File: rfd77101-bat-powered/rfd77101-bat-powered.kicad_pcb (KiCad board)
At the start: 2 copper layers, 23 parts, among them J1 USB_OTG, J2 BATT_CONN, J3 Conn_01x07, Q1 Q_NMOS_GSD, Q2 Q_PMOS_GSD, U1 RFD77101, U2 MCP73811T-420I-OT, U3 TLV74130

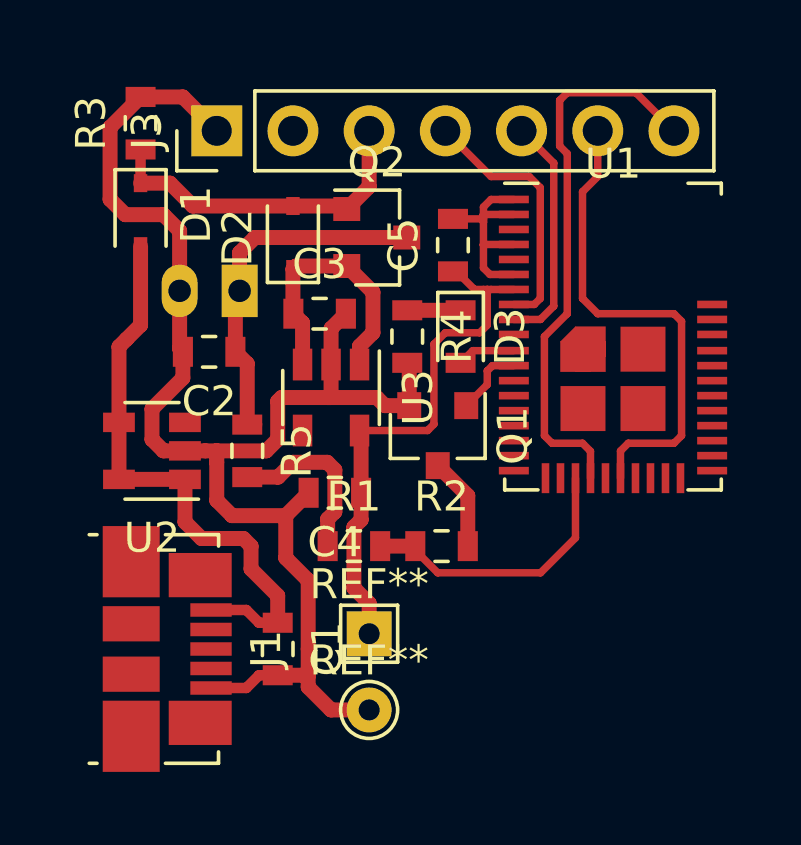
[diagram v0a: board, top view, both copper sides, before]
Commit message: update board for better batt measurements
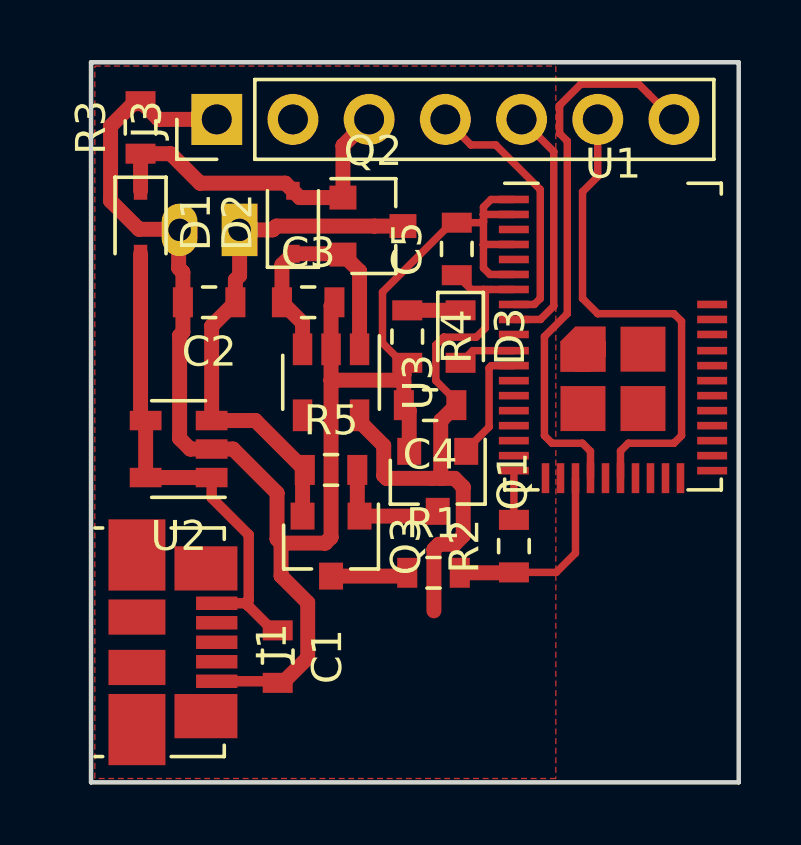
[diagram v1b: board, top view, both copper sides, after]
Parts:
- removed REF**: TestPoint_THTPad_D1.5mm_Drill0.7mm, TestPoint:TestPoint_THTPad_D1.5mm_Drill0.7mm
- removed REF**: TestPoint_THTPad_1.5x1.5mm_Drill0.7mm, TestPoint:TestPoint_THTPad_1.5x1.5mm_Drill0.7mm
- added Q3: DMP3099L-13, Package_TO_SOT_SMD:SOT-23, F.Cu at (149.6, 104.0)
- J1: value USB_OTG -> USB_B_Micro
- Q2: value Q_PMOS_GSD -> DMP3099L-13
- R1: value 1.6k -> 3.1k
- R5: value 1.6k -> 10k
- moved C4 4.31 mm to (152.9, 99.3)
- moved R5 2.87 mm to (149.6, 101.5), turned to 0 degrees
- moved R1 2.80 mm to (153.0, 104.9)
- moved R2 2.41 mm to (155.7, 104.0), turned to 90 degrees
- moved J2 2.03 mm to (146.6, 93.5)
- moved C2 1.65 mm to (145.5, 95.9)
- moved Q1 1.52 mm to (153.2, 101.9)
- moved U2 0.89 mm to (144.5, 100.8)
- moved C3 0.54 mm to (148.8, 95.9)
- moved D2 0.51 mm to (148.3, 93.2)
- moved U3 0.51 mm to (149.6, 98.6)
- moved Q2 0.40 mm to (151.0, 93.3)
- moved J3 0.38 mm to (145.8, 89.8)
- moved J1 0.29 mm to (144.3, 107.2)
- moved C1 0.25 mm to (147.8, 107.7)
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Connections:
- R1 pad 1: Net-(R1-Pad1) -> Net-(Q3-Pad3)
- R2 pad 2: Net-(Q1-Pad3) -> GND
- R5 pad 2: Net-(R1-Pad1) -> Net-(Q1-Pad3)
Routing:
- net +BATT: track 11.9 -> 18.0 mm
- net Net-(R1-Pad1): track 5.87 -> 0.00 mm
- net GND: track 56.8 -> 60.1 mm
- net /BATT_V: track 9.43 -> 6.63 mm
- net VDD: track 17.8 -> 20.5 mm
- net Net-(Q3-Pad3): track 0.00 -> 2.59 mm
- net Net-(C1-Pad1): track 19.4 -> 17.0 mm
- net /BATT_V_EN: track 2.41 -> 3.95 mm
- net Net-(Q1-Pad3): track 3.26 -> 4.24 mm
- added copper zone on F.Cu, net GND
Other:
- board outline added: 21.6 x 24 mm
